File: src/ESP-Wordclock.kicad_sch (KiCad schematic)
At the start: 1 part

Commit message: Add: Vendor no. and footprints
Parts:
- R101: footprint (none) -> Resistor_SMD:R_0805_2012Metric_Pad1.20x1.40mm_HandSolder; Manufacturer (none) -> -; Manufacturer Part no. (none) -> -; Vendor 1 (none) -> Digikey; Vendor 1 Part no. (none) -> 311-0.0ARCT-ND; Vendor 2 (none) -> LCSC
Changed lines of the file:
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@@
 			)
 		)
-		(property "Footprint" ""
+		(property "Footprint" "Resistor_SMD:R_0805_2012Metric_Pad1.20x1.40mm_HandSolder"
 			(at 166.878 116.84 90)
 			(effects
@@
 			)
 		)
-		(property "Manufacturer" ""
+		(property "Manufacturer" "-"
 			(at 165.1 116.84 0)
 			(effects
@@
 			)
 		)
-		(property "Manufacturer Part no." ""
+		(property "Manufacturer Part no." "-"
 			(at 165.1 116.84 0)
 			(effects
@@
 			)
 		)
-		(property "Vendor 1" ""
+		(property "Vendor 1" "Digikey"
 			(at 165.1 116.84 0)
 			(effects
@@
 			)
 		)
-		(property "Vendor 1 Part no." ""
+		(property "Vendor 1 Part no." "311-0.0ARCT-ND"
 			(at 165.1 116.84 0)
 			(effects
@@
 			)
 		)
-		(property "Vendor 2" ""
+		(property "Vendor 2" "LCSC"
 			(at 165.1 116.84 0)
 			(effects

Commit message: Mod: Changed parts to match with both vendors
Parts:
- R101: Manufacturer - -> YAGEO; Manufacturer Part no. - -> RC0805JR-070RL; Vendor 2 Part no. (none) -> C96345
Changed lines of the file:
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@@
 	(title_block
 		(title "Wordclock - Top")
-		(date "2024-10-27")
+		(date "2024-10-29")
 		(rev "A")
 		(company "ElektroNik Zoller")
@@
 			)
 		)
-		(property "Manufacturer" "-"
-			(at 165.1 116.84 0)
-			(effects
-				(font
-					(size 1.27 1.27)
-				)
-				(hide yes)
-			)
-		)
-		(property "Manufacturer Part no." "-"
+		(property "Manufacturer" "YAGEO"
+			(at 165.1 116.84 0)
+			(effects
+				(font
+					(size 1.27 1.27)
+				)
+				(hide yes)
+			)
+		)
+		(property "Manufacturer Part no." "RC0805JR-070RL"
 			(at 165.1 116.84 0)
 			(effects
@@
 			)
 		)
-		(property "Vendor 2 Part no." ""
-			(at 165.1 116.84 0)
-			(effects
+		(property "Vendor 2 Part no." "C96345"
+			(at 165.1 116.84 0)
+			(effects

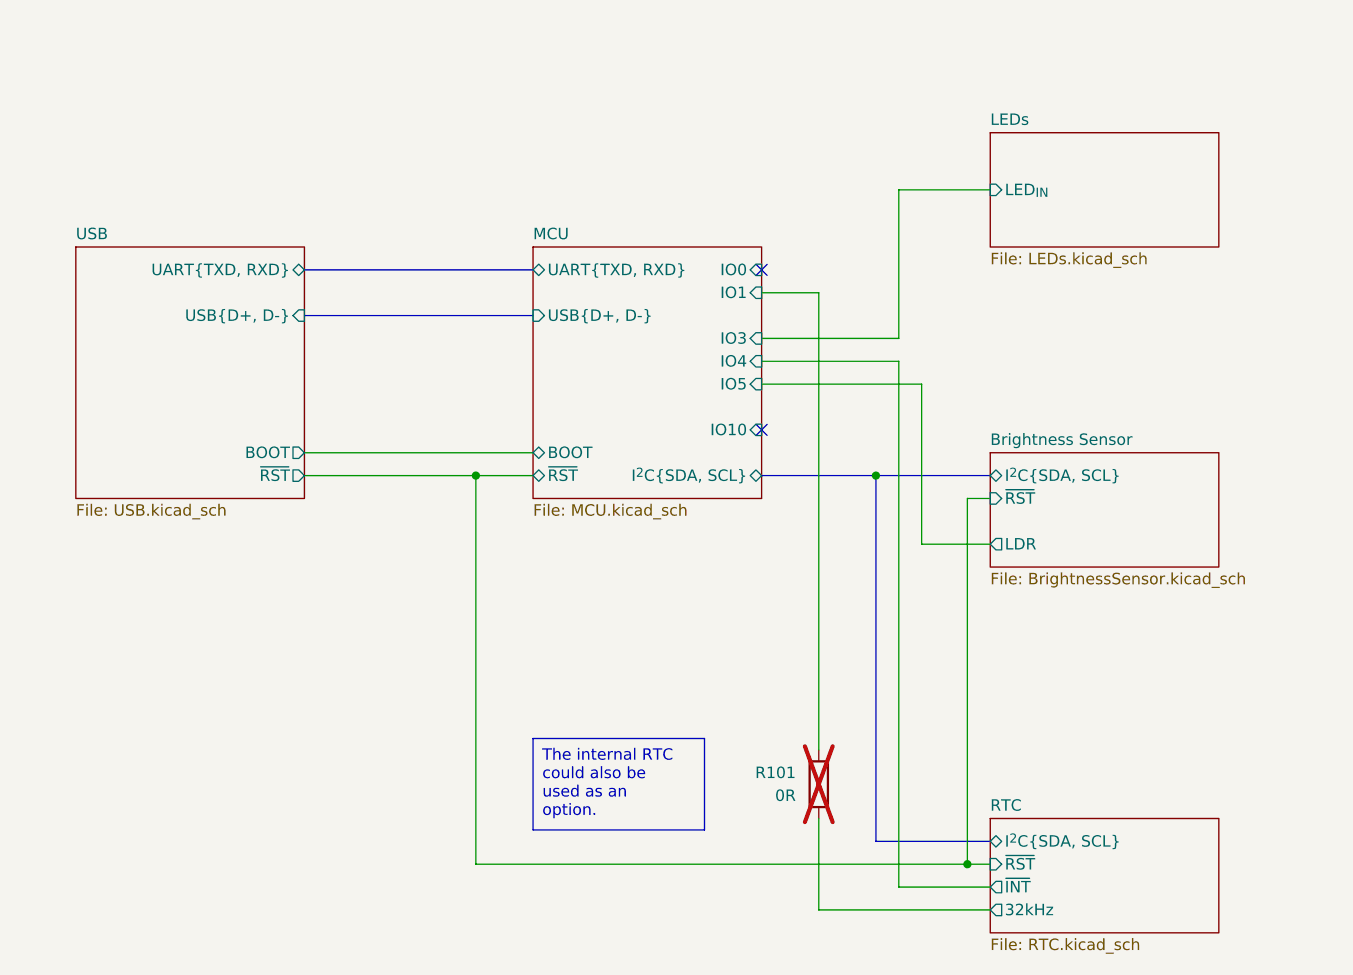
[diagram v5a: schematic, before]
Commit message: Add: Header for empty pins of the ESP32 and added more 0R resistors to break up some connections
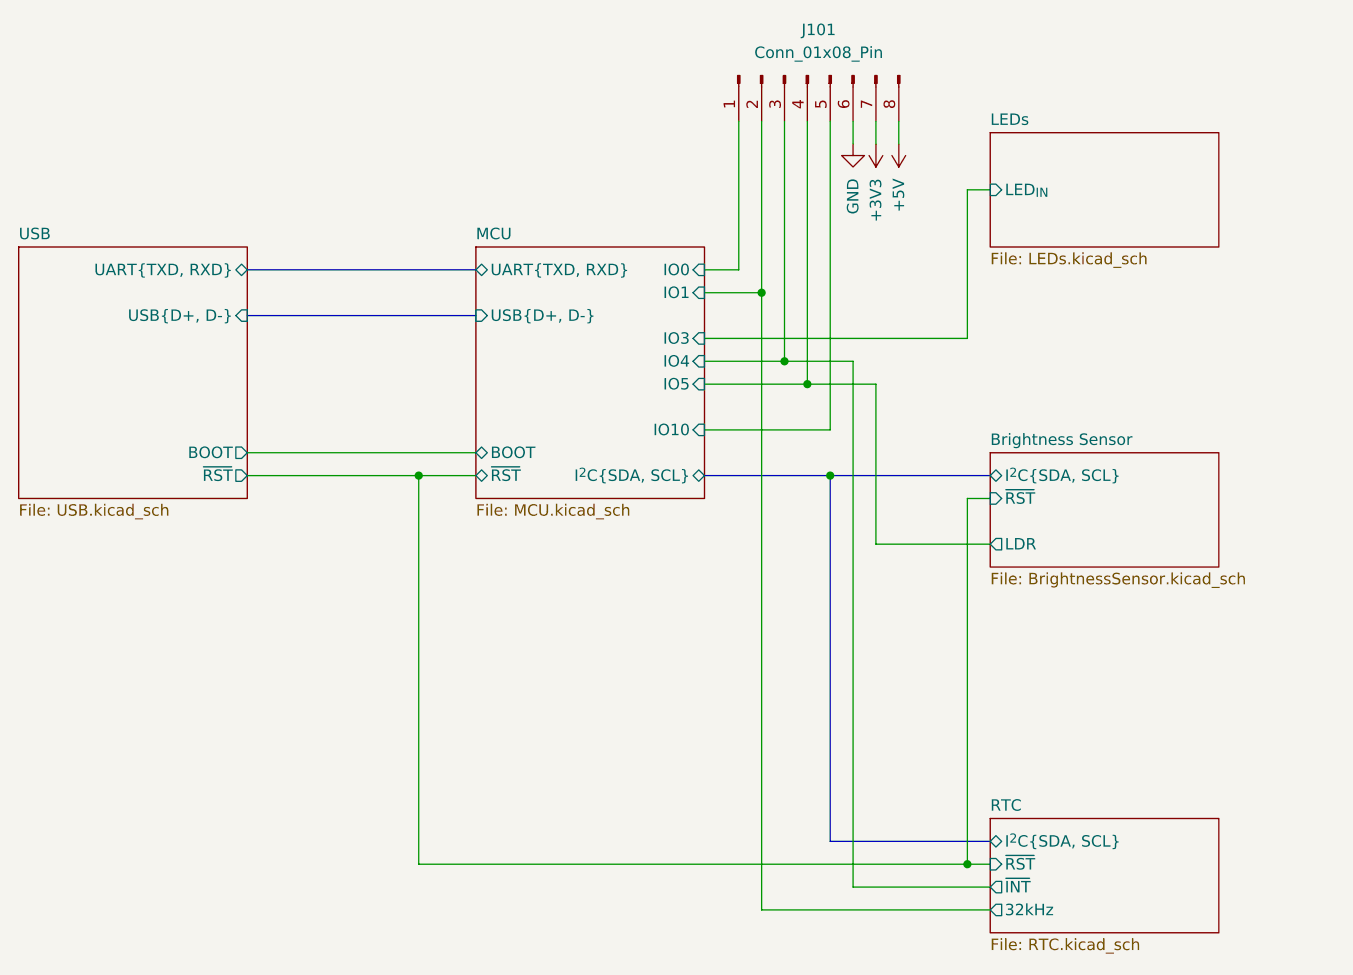
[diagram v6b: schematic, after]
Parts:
- removed R101: 0R, Resistor_SMD:R_0805_2012Metric_Pad1.20x1.40mm_HandSolder, symbol Device:R
- added J101: Conn_01x08_Pin, symbol Connector:Conn_01x08_Pin
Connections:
- net Brightness Sensor/LDR: now also J101.4 (Pin_4)
- net MCU/IO0: now also J101.1 (Pin_1)
- net MCU/IO1: now also J101.2 (Pin_2)
- net MCU/IO10: now also J101.5 (Pin_5)
- net MCU/IO4: now also J101.3 (Pin_3)
- new net +3V3: J101.7 (Pin_7)
- new net +5V: J101.8 (Pin_8)
- new net GND: J101.6 (Pin_6)
- no-connect marks 2 -> 0

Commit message: Fix: Name of the battery cell. Run ERC and created finished schematic, ready for the layout
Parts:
- J101: footprint (none) -> Connector_PinHeader_2.54mm:PinHeader_1x08_P2.54mm_Vertical; Manufacturer (none) -> -; Manufacturer Part no. (none) -> -; Vendor 1 (none) -> -; Vendor 1 Part no. (none) -> -; Vendor 2 (none) -> -; Vendor 2 Part no. (none) -> -
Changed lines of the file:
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@@
 		(on_board yes)
 		(dnp no)
-		(property "Reference" "#PWR0103"
+		(property "Reference" "#PWR0102"
 			(at 171.45 41.91 0)
 			(effects
@@
 			(project ""
 				(path "/bfaac094-0365-40a4-8b7a-d4d62ace544e"
-					(reference "#PWR0103")
+					(reference "#PWR0102")
 					(unit 1)
 				)
@@
 			)
 		)
-		(property "Footprint" ""
+		(property "Footprint" "Connector_PinHeader_2.54mm:PinHeader_1x08_P2.54mm_Vertical"
 			(at 163.83 38.1 0)
 			(effects
@@
 		)
 		(property "Description" "Generic connector, single row, 01x08, script generated"
+			(at 163.83 38.1 0)
+			(effects
+				(font
+					(size 1.27 1.27)
+				)
+				(hide yes)
+			)
+		)
+		(property "Manufacturer" "-"
+			(at 163.83 38.1 0)
+			(effects
+				(font
+					(size 1.27 1.27)
+				)
+				(hide yes)
+			)
+		)
+		(property "Manufacturer Part no." "-"
+			(at 163.83 38.1 0)
+			(effects
+				(font
+					(size 1.27 1.27)
+				)
+				(hide yes)
+			)
+		)
+		(property "Vendor 1" "-"
+			(at 163.83 38.1 0)
+			(effects
+				(font
+					(size 1.27 1.27)
+				)
+				(hide yes)
+			)
+		)
+		(property "Vendor 1 Part no." "-"
+			(at 163.83 38.1 0)
+			(effects
+				(font
+					(size 1.27 1.27)
+				)
+				(hide yes)
+			)
+		)
+		(property "Vendor 2" "-"
+			(at 163.83 38.1 0)
+			(effects
+				(font
+					(size 1.27 1.27)
+				)
+				(hide yes)
+			)
+		)
+		(property "Vendor 2 Part no." "-"
 			(at 163.83 38.1 0)
 			(effects
@@
 		(on_board yes)
 		(dnp no)
-		(property "Reference" "#PWR0102"
+		(property "Reference" "#PWR0103"
 			(at 173.99 41.91 0)
 			(effects
@@
 			(project ""
 				(path "/bfaac094-0365-40a4-8b7a-d4d62ace544e"
-					(reference "#PWR0102")
+					(reference "#PWR0103")
 					(unit 1)
 				)

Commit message: Mod: Layout, finished the layout. Changed the voltage pins of J101
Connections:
- net +3V3: now also J101.8 (Pin_8); no longer J101.7 (Pin_7)
- net +5V: now also J101.7 (Pin_7); no longer J101.8 (Pin_8)
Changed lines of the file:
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@@
 	(symbol
 		(lib_id "power:+3V3")
-		(at 171.45 45.72 180)
+		(at 173.99 45.72 180)
 		(unit 1)
 		(exclude_from_sim no)
@@
 		(dnp no)
 		(property "Reference" "#PWR0102"
-			(at 171.45 41.91 0)
+			(at 173.99 41.91 0)
 			(effects
 				(font
@@
 		)
 		(property "Value" "+3V3"
-			(at 171.45 49.53 90)
+			(at 173.99 49.53 90)
 			(effects
 				(font
@@
 		)
 		(property "Footprint" ""
-			(at 171.45 45.72 0)
+			(at 173.99 45.72 0)
 			(effects
 				(font
@@
 		)
 		(property "Datasheet" ""
-			(at 171.45 45.72 0)
+			(at 173.99 45.72 0)
 			(effects
 				(font
@@
 		)
 		(property "Description" "Power symbol creates a global label with name \"+3V3\""
-			(at 171.45 45.72 0)
+			(at 173.99 45.72 0)
 			(effects
 				(font
@@
 	(symbol
 		(lib_id "power:+5V")
-		(at 173.99 45.72 180)
+		(at 171.45 45.72 180)
 		(unit 1)
 		(exclude_from_sim no)
@@
 		(dnp no)
 		(property "Reference" "#PWR0103"
-			(at 173.99 41.91 0)
+			(at 171.45 41.91 0)
 			(effects
 				(font
@@
 		)
 		(property "Value" "+5V"
-			(at 173.99 49.53 90)
+			(at 171.45 49.53 90)
 			(effects
 				(font
@@
 		)
 		(property "Footprint" ""
-			(at 173.99 45.72 0)
+			(at 171.45 45.72 0)
 			(effects
 				(font
@@
 		)
 		(property "Datasheet" ""
-			(at 173.99 45.72 0)
+			(at 171.45 45.72 0)
 			(effects
 				(font
@@
 		)
 		(property "Description" "Power symbol creates a global label with name \"+5V\""
-			(at 173.99 45.72 0)
-			(effects
-				(font
+			(at 171.45 45.72 0)
+			(effects
+				(font
